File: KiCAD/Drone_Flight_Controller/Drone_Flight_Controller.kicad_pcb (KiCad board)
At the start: 2 copper layers, 0 parts

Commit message: Routing and placing
Routing and placing
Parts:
- added +5V1: +5V, TestPoint:TestPoint_Pad_D1.0mm, F.Cu at (128.4, 56.9)
- added 3V1: 3V3, TestPoint:TestPoint_Pad_D1.0mm, F.Cu at (128.4, 60.0)
- added BZ1: Buzzer, Buzzer_Beeper:Buzzer_TDK_PS1240P02BT_D12.2mm_H6.5mm, F.Cu at (149.0, 74.9)
- added C1: 22u, Capacitor_THT:CP_Radial_D5.0mm_P2.00mm, F.Cu at (139.0, 71.5)
- added C10: 100nF, Capacitor_SMD:C_0805_2012Metric, B.Cu at (170.6, 80.0)
- added C11: 100nF, Capacitor_SMD:C_0805_2012Metric, F.Cu at (153.1, 64.1)
- added C12: 10uF, Capacitor_SMD:C_0805_2012Metric, B.Cu at (181.4, 62.1)
- added C13: 10uF, Capacitor_SMD:C_0805_2012Metric, B.Cu at (187.1, 62.1)
- added C14: 100nF, Capacitor_SMD:C_0805_2012Metric, F.Cu at (171.2, 64.1)
- added C2: 100nF, Capacitor_SMD:C_0805_2012Metric, B.Cu at (156.0, 68.4)
- added C3: 10uF, Capacitor_SMD:C_0805_2012Metric, F.Cu at (186.3, 62.8)
- added C4: 1uF, Capacitor_SMD:C_0805_2012Metric_Pad1.18x1.45mm_HandSolder, B.Cu at (157.7, 76.5)
- added C5: 10uF, Capacitor_SMD:C_0805_2012Metric, B.Cu at (160.0, 68.4)
- added C6: 100nF, Capacitor_SMD:C_0805_2012Metric, F.Cu at (186.3, 60.8)
- added C7: 120n, Capacitor_SMD:C_0805_2012Metric_Pad1.18x1.45mm_HandSolder, B.Cu at (163.1, 72.5)
- added C8: 10uF, Capacitor_SMD:C_0805_2012Metric, B.Cu at (186.7, 82.7)
- added C9: 100nF, Capacitor_SMD:C_0805_2012Metric, B.Cu at (181.2, 82.7)
- added D1: BAT60BE6359HTMA1, Diode_SMD:D_SOD-323_HandSoldering, B.Cu at (164.7, 62.1)
- added D10: LED, LED_SMD:LED_0805_2012Metric_Pad1.15x1.40mm_HandSolder, F.Cu at (161.3, 91.5)
- added D11: LED, LED_SMD:LED_0805_2012Metric_Pad1.15x1.40mm_HandSolder, F.Cu at (164.6, 91.5)
- added D12: LED, LED_SMD:LED_0805_2012Metric_Pad1.15x1.40mm_HandSolder, F.Cu at (167.9, 91.5)
- added D13: LED, LED_SMD:LED_0805_2012Metric_Pad1.15x1.40mm_HandSolder, F.Cu at (171.2, 91.5)
- added D15: LED, LED_SMD:LED_0805_2012Metric_Pad1.15x1.40mm_HandSolder, F.Cu at (155.3, 52.4)
- added D19: LED, LED_SMD:LED_0805_2012Metric_Pad1.15x1.40mm_HandSolder, F.Cu at (151.4, 91.5)
- added D2: BAT60BE6359HTMA1, Diode_SMD:D_SOD-323_HandSoldering, F.Cu at (132.7, 57.0)
- added D3: BAT60BE6359HTMA1, Diode_SMD:D_SOD-323_HandSoldering, F.Cu at (132.7, 88.0)
- added D4: LED, LED_SMD:LED_0805_2012Metric_Pad1.15x1.40mm_HandSolder, F.Cu at (144.8, 91.5)
- added D5: LED, LED_SMD:LED_0805_2012Metric_Pad1.15x1.40mm_HandSolder, F.Cu at (148.1, 91.5)
- added D6: BAT60BE6359HTMA1, Diode_SMD:D_SOD-323_HandSoldering, F.Cu at (183.3, 57.0)
- added D7: BAT60BE6359HTMA1, Diode_SMD:D_SOD-323_HandSoldering, F.Cu at (183.4, 87.9)
- added D8: LED, LED_SMD:LED_0805_2012Metric_Pad1.15x1.40mm_HandSolder, F.Cu at (154.7, 91.5)
- added D9: LED, LED_SMD:LED_0805_2012Metric_Pad1.15x1.40mm_HandSolder, F.Cu at (158.0, 91.5)
- added F1: PTS12066V050, Fuse:Fuse_1206_3216Metric, B.Cu at (159.4, 62.3)
- added F2: PTS12066V050, Fuse:Fuse_1206_3216Metric, F.Cu at (134.9, 57.4)
- added F3: PTS12066V050, Fuse:Fuse_1206_3216Metric, F.Cu at (134.9, 87.7)
- added F4: PTS12066V050, Fuse:Fuse_1206_3216Metric, F.Cu at (181.1, 57.4)
- added F5: PTS12066V050, Fuse:Fuse_1206_3216Metric, F.Cu at (181.2, 87.6)
- added FID1: Fiducial, Fiducial:Fiducial_0.5mm_Mask1mm, F.Cu at (130.6, 58.6)
- added FID2: Fiducial, Fiducial:Fiducial_0.5mm_Mask1mm, F.Cu at (187.0, 87.3)
- added G1: Logo_HTL_Steyr_Small, Symbol_:HTL-Steyr-Logo_5mm_Copper, F.Cu at (369.0, 105.5)
- added GND1: GND, TestPoint:TestPoint_Pad_D1.0mm, F.Cu at (128.4, 63.0)
- added GPS1: Conn_01x04, Connector_PinHeader_2.54mm:PinHeader_1x04_P2.54mm_Vertical, F.Cu at (148.0, 53.0)
- added H1: MountingHole_Pad, MountingHole:MountingHole_2.2mm_M2_Pad_TopBottom, F.Cu at (129.0, 53.5)
- added H2: MountingHole_Pad, MountingHole:MountingHole_2.2mm_M2_Pad_TopBottom, F.Cu at (187.0, 53.5)
- added H3: MountingHole_Pad, MountingHole:MountingHole_2.2mm_M2_Pad_TopBottom, F.Cu at (129.0, 91.5)
- added H4: MountingHole_Pad, MountingHole:MountingHole_2.2mm_M2_Pad_TopBottom, F.Cu at (187.0, 91.5)
- added J1: XT60, Connector_AMASS:AMASS_XT60-F_1x02_P7.20mm_Vertical, F.Cu at (131.5, 76.6)
- added J2: 0.5mΩ high side shunt, Connector_PinHeader_2.54mm:PinHeader_1x02_P2.54mm_Vertical, F.Cu at (144.0, 53.0)
- added J3: Micro_SD_Card, Connector_Card:microSD_HC_Hirose_DM3D-SF, B.Cu at (147.4, 87.2)
- added Motor1: Conn_01x03, Connector_PinHeader_2.54mm:PinHeader_1x03_P2.54mm_Vertical, F.Cu at (133.5, 53.0)
- added Motor2: Conn_01x03, Connector_PinHeader_2.54mm:PinHeader_1x03_P2.54mm_Vertical, F.Cu at (177.5, 53.0)
- added Motor3: Conn_01x03, Connector_PinHeader_2.54mm:PinHeader_1x03_P2.54mm_Vertical, F.Cu at (133.5, 92.0)
- added Motor4: Conn_01x03, Connector_PinHeader_2.54mm:PinHeader_1x03_P2.54mm_Vertical, F.Cu at (177.5, 92.0)
- added Q1: 2N2222A, Package_TO_SOT_THT:TO-92_HandSolder, F.Cu at (138.6, 65.2)
- added R1: 5k1, Resistor_SMD:R_0805_2012Metric_Pad1.20x1.40mm_HandSolder, F.Cu at (158.7, 63.0)
- added R10: 10k, Resistor_SMD:R_0805_2012Metric_Pad1.20x1.40mm_HandSolder, B.Cu at (166.6, 80.0)
- added R11: 220, Resistor_SMD:R_0805_2012Metric_Pad1.20x1.40mm_HandSolder, B.Cu at (170.6, 76.0)
- added R12: 10k, Resistor_SMD:R_0805_2012Metric_Pad1.20x1.40mm_HandSolder, F.Cu at (153.0, 52.4)
- added R13: 3k6, Resistor_SMD:R_0805_2012Metric_Pad1.20x1.40mm_HandSolder, F.Cu at (168.9, 52.4)
- added R14: 1k8, Resistor_SMD:R_0805_2012Metric_Pad1.20x1.40mm_HandSolder, F.Cu at (154.7, 86.5)
- added R15: 1k8, Resistor_SMD:R_0805_2012Metric_Pad1.20x1.40mm_HandSolder, F.Cu at (158.0, 86.5)
- added R16: 1k8, Resistor_SMD:R_0805_2012Metric_Pad1.20x1.40mm_HandSolder, F.Cu at (161.3, 86.5)
- added R17: 1k8, Resistor_SMD:R_0805_2012Metric_Pad1.20x1.40mm_HandSolder, F.Cu at (164.6, 86.6)
- added R18: 1k8, Resistor_SMD:R_0805_2012Metric_Pad1.20x1.40mm_HandSolder, F.Cu at (167.9, 86.5)
- added R19: 1k8, Resistor_SMD:R_0805_2012Metric_Pad1.20x1.40mm_HandSolder, F.Cu at (171.2, 86.5)
- added R2: 5k1, Resistor_SMD:R_0805_2012Metric_Pad1.20x1.40mm_HandSolder, F.Cu at (165.6, 63.0)
- added R24: 1k8, Resistor_SMD:R_0805_2012Metric_Pad1.20x1.40mm_HandSolder, F.Cu at (151.4, 86.5)
- added R25: 10k, Resistor_SMD:R_0805_2012Metric_Pad1.20x1.40mm_HandSolder, B.Cu at (141.6, 78.1)
- added R26: 10k, Resistor_SMD:R_0805_2012Metric_Pad1.20x1.40mm_HandSolder, B.Cu at (144.6, 78.1)
- added R27: 10k, Resistor_SMD:R_0805_2012Metric_Pad1.20x1.40mm_HandSolder, B.Cu at (147.5, 78.1)
- added R28: 10k, Resistor_SMD:R_0805_2012Metric_Pad1.20x1.40mm_HandSolder, B.Cu at (150.4, 78.1)
- added R29: 10k, Resistor_SMD:R_0805_2012Metric_Pad1.20x1.40mm_HandSolder, B.Cu at (153.4, 78.1)
- added R3: 180, Resistor_SMD:R_0805_2012Metric_Pad1.20x1.40mm_HandSolder, B.Cu at (148.5, 66.5)
- added R4: 1k, Resistor_SMD:R_0805_2012Metric_Pad1.20x1.40mm_HandSolder, B.Cu at (143.5, 66.5)
- added R5: 1k8, Resistor_SMD:R_0805_2012Metric_Pad1.20x1.40mm_HandSolder, F.Cu at (144.8, 86.5)
- added R6: 3k6, Resistor_SMD:R_0805_2012Metric_Pad1.20x1.40mm_HandSolder, F.Cu at (148.1, 86.5)
- added R7: 10k, Resistor_SMD:R_0805_2012Metric_Pad1.20x1.40mm_HandSolder, B.Cu at (162.1, 76.5)
- added R8: 10k, Resistor_SMD:R_0805_2012Metric_Pad1.20x1.40mm_HandSolder, F.Cu at (171.2, 52.4)
- added R9: 43k, Resistor_SMD:R_0805_2012Metric_Pad1.20x1.40mm_HandSolder, B.Cu at (166.6, 76.0)
- added SW1: SW_Push, htl_smd:SW_Push_5.1mm_H1.5mm, F.Cu at (171.2, 58.1)
- added SW2: SW_Push, htl_smd:SW_Push_5.1mm_H1.5mm, F.Cu at (153.1, 58.1)
- added U1: 74AHC1G125, Package_TO_SOT_SMD:SOT-353_SC-70-5, F.Cu at (137.8, 56.5)
- added U2: 74AHC1G125, Package_TO_SOT_SMD:SOT-353_SC-70-5, F.Cu at (137.7, 88.6)
- added U3: 74AHC1G125, Package_TO_SOT_SMD:SOT-353_SC-70-5, F.Cu at (178.2, 56.4)
- added U4: 74AHC1G125, Package_TO_SOT_SMD:SOT-353_SC-70-5, F.Cu at (178.3, 88.5)
- added U5: BNO055, Package_LGA:LGA-28_5.2x3.8mm_P0.5mm, B.Cu at (158.0, 72.5)
- added U6: ESP32-S3-MINI-1, RF_Module_:ESP32-S3-MINI-1, F.Cu at (181.3, 72.5)
- added U7: DPS368, Package_LGA:Bosch_LGA-8_2x2.5mm_P0.65mm_ClockwisePinNumbering, B.Cu at (184.0, 82.7)
- added U8: TLV75533PDBV, Package_TO_SOT_SMD:SOT-23-5, B.Cu at (184.2, 62.1)
- added U9: INA195, Package_TO_SOT_SMD:SOT-23-5, B.Cu at (143.0, 60.0)
- added USB-C1: USB_C_Receptacle_USB2.0_14P, Connector_USB:USB_C_Receptacle_HRO_TYPE-C-31-M-12, F.Cu at (162.1, 54.4)
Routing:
- net +3V3: track 0.00 -> 204.1 mm, vias 0 -> 3
- net +5V: track 0.00 -> 200.2 mm, vias 0 -> 2
- net SDI: track 0.00 -> 73.4 mm, vias 0 -> 3
- net Motor3: track 0.00 -> 71.3 mm, vias 0 -> 2
- net SDO: track 0.00 -> 64.7 mm, vias 0 -> 3
- net Motor1: track 0.00 -> 56.9 mm, vias 0 -> 4
- net SD_CS: track 0.00 -> 55.1 mm, vias 0 -> 1
- net EN: track 0.00 -> 53.9 mm, vias 0 -> 2
- net SCK: track 0.00 -> 53.0 mm, vias 0 -> 4
- net LED6: track 0.00 -> 48.1 mm, vias 0 -> 2
- net LED5: track 0.00 -> 46.5 mm, vias 0 -> 2
- net LED4: track 0.00 -> 44.2 mm, vias 0 -> 2
- net CurrentSense: track 0.00 -> 43.7 mm, vias 0 -> 1
- net LED7: track 0.00 -> 43.6 mm, vias 0 -> 2
- net LED3: track 0.00 -> 41.7 mm, vias 0 -> 2
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- added copper zone on B.Cu, net GND
- added copper zone on F.Cu, net GND
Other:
- board outline added: 65 x 45 mm

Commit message: Revision
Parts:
- moved +5V 0.72 mm to (129.0, 57.3)
- moved 3V3 0.72 mm to (129.0, 60.4)
- moved GND 0.72 mm to (129.0, 63.4)
- moved U7 0.10 mm to (183.9, 82.8)
- renumbered +5V1 to +5V, 3V1 to 3V3, GND1 to GND
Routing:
- net +3V3: track 204.1 -> 200.0 mm

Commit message: Add signage
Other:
- board text added: "3V3"
- board text added: "5V"
- board text added: "BOOT"
- board text added: "RESET"

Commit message: routing
routing
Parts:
- moved F3 4.77 mm to (139.5, 86.7)
- moved F2 4.71 mm to (139.5, 58.3)
- moved D3 4.48 mm to (137.0, 87.0)
- moved D2 4.44 mm to (137.0, 58.0)
- moved U2 4.27 mm to (133.6, 87.6), turned to 0 degrees
- moved U1 4.27 mm to (133.6, 57.4), turned to 0 degrees
- moved F4 2.59 mm to (183.5, 58.3)
- moved D7 2.53 mm to (181.0, 87.0)
- moved F5 2.50 mm to (183.5, 86.7)
- moved D6 2.48 mm to (181.0, 58.0)
- moved R8 2.00 mm to (173.1, 53.1)
- moved R12 1.84 mm to (151.3, 53.1)
- moved FID1 1.72 mm to (130.8, 60.3)
- moved R3 1.50 mm to (147.0, 66.5)
- moved U3 1.22 mm to (177.5, 57.4)
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- renumbered GPS1 to GPS, USB-C1 to USB-C
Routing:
- net +5V: track 199.7 -> 180.4 mm
- net GPS TX: track 34.1 -> 40.2 mm
- net GPS RX: track 32.9 -> 38.1 mm
- net Motor1: track 56.9 -> 62.0 mm
- net Net-(Motor3-Pin_1): track 9.30 -> 4.18 mm, vias 1 -> 0
- net +3V3: track 200.0 -> 204.9 mm
- net Net-(Motor4-Pin_1): track 8.77 -> 4.18 mm, vias 1 -> 0
- net Net-(Motor1-Pin_1): track 10.1 -> 5.73 mm, vias 1 -> 0
- net Motor3: track 71.3 -> 74.7 mm, vias 2 -> 4
- net Net-(C14-Pad1): track 12.4 -> 10.4 mm
- net Net-(Q1-B): track 9.06 -> 7.06 mm
- net Buzzer: track 29.5 -> 31.5 mm
- net Net-(Motor2-Pin_1): track 7.17 -> 5.56 mm, vias 1 -> 0
- net Net-(BZ1--): track 15.2 -> 13.6 mm
- net D-: track 23.5 -> 25.0 mm
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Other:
- board text removed: "BOOT"

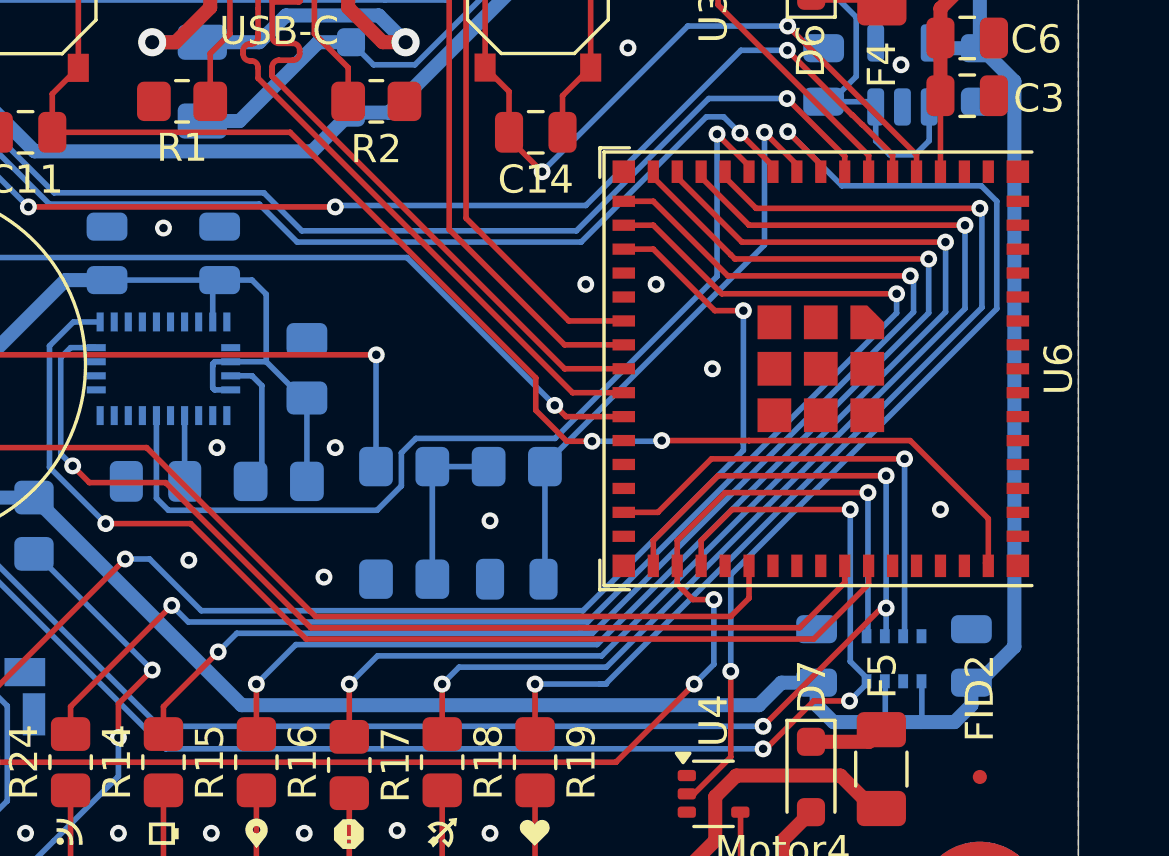
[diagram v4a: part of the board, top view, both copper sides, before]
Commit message: Shorten traces
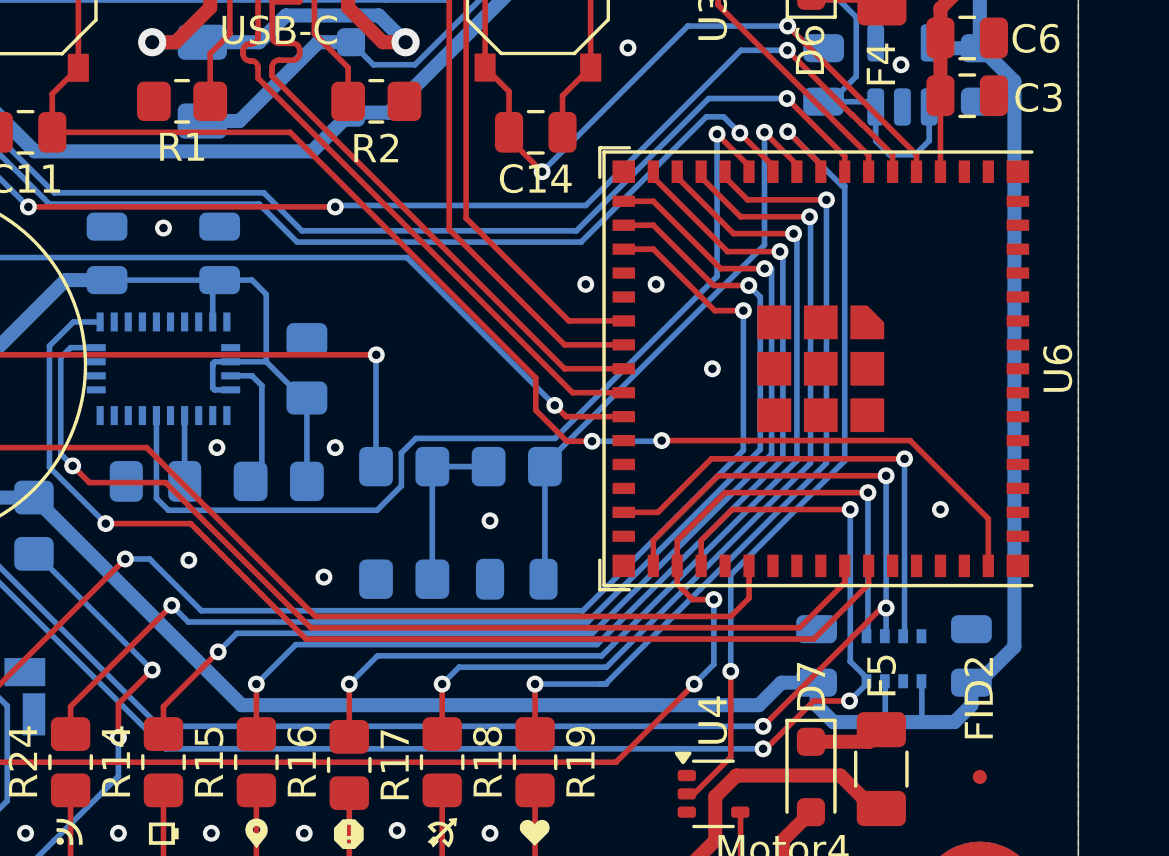
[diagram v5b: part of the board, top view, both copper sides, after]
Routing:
- net LED1: track 36.7 -> 29.1 mm
- net LED2: track 39.1 -> 31.7 mm
- net Motor4: track 36.1 -> 28.8 mm
- net LED4: track 44.2 -> 37.0 mm
- net LED3: track 41.7 -> 34.6 mm
- net LED6: track 48.1 -> 41.1 mm
- net LED5: track 46.5 -> 39.6 mm

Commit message: Update Signage
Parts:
- removed G1: Logo_HTL_Steyr_Small, Symbol_:HTL-Steyr-Logo_5mm_Copper
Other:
- board text added: "Flight Controller V3 Brandner, Hinterberger TOP GND"

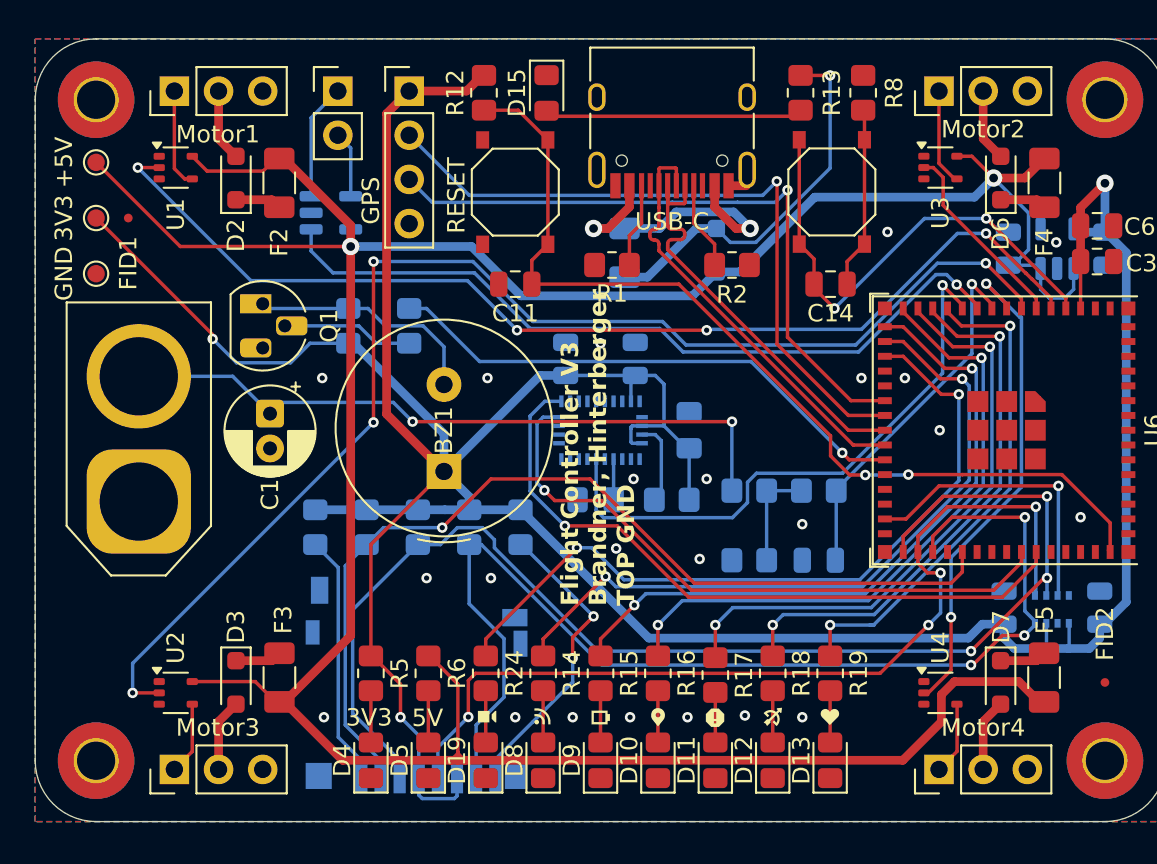
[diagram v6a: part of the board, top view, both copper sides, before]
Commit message: Mark GND on connectors
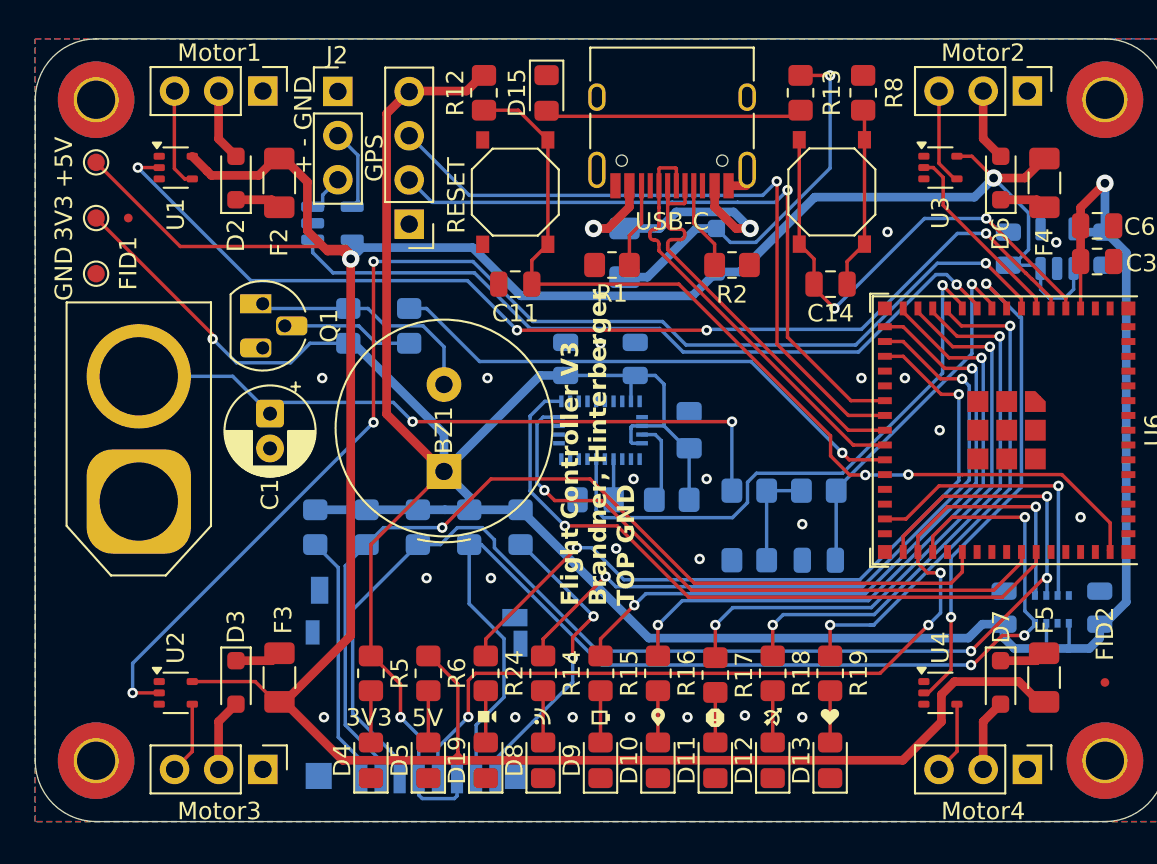
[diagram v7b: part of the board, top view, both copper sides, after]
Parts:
- J2: footprint Connector_PinHeader_2.54mm:PinHeader_1x02_P2.54mm_Vertical -> Connector_PinHeader_2.54mm:PinHeader_1x03_P2.54mm_Vertical
- moved GPS 7.65 mm to (147.0, 60.6), turned to 180 degrees
- moved Motor1 5.09 mm to (138.6, 53.0), turned to -90 degrees
- moved Motor3 5.09 mm to (138.6, 92.0), turned to -90 degrees
- moved Motor2 5.08 mm to (182.5, 53.0), turned to -90 degrees
- moved Motor4 5.08 mm to (182.5, 92.0), turned to -90 degrees
- moved U9 0.61 mm to (142.6, 60.6)
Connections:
- GPS pad 1: +3V3 -> GND
- GPS pad 2: GPS TX -> GPS RX
- GPS pad 3: GPS RX -> GPS TX
- GPS pad 4: GND -> +3V3
- J2 pad 1: Net-(J2-Pin_1) -> GND
- Motor1 pad 1: Net-(Motor1-Pin_1) -> GND
- Motor1 pad 3: GND -> Net-(Motor1-Pin_3)
- Motor2 pad 1: Net-(Motor2-Pin_1) -> GND
- Motor2 pad 3: GND -> Net-(Motor2-Pin_3)
- Motor3 pad 1: Net-(Motor3-Pin_1) -> GND
- Motor3 pad 3: GND -> Net-(Motor3-Pin_3)
- Motor4 pad 1: Net-(Motor4-Pin_1) -> GND
- Motor4 pad 3: GND -> Net-(Motor4-Pin_3)
- U1 pad 4: Net-(Motor1-Pin_1) -> Net-(Motor1-Pin_3)
- U2 pad 4: Net-(Motor3-Pin_1) -> Net-(Motor3-Pin_3)
- U3 pad 4: Net-(Motor2-Pin_1) -> Net-(Motor2-Pin_3)
- U4 pad 4: Net-(Motor4-Pin_1) -> Net-(Motor4-Pin_3)
- U9 pad 3: Net-(J2-Pin_1) -> Net-(J2-Pin_3)
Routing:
- net Net-(J2-Pin_1): track 7.49 -> 0.00 mm
- net Net-(Motor1-Pin_3): track 0.00 -> 5.73 mm
- net Net-(Motor1-Pin_1): track 5.73 -> 0.00 mm
- net Net-(Motor2-Pin_3): track 0.00 -> 5.56 mm
- net Net-(Motor2-Pin_1): track 5.56 -> 0.00 mm
- net Net-(Motor4-Pin_3): track 0.00 -> 4.18 mm
- net Net-(Motor4-Pin_1): track 4.18 -> 0.00 mm
- net Net-(Motor3-Pin_3): track 0.00 -> 4.18 mm
- net Net-(Motor3-Pin_1): track 4.18 -> 0.00 mm
- net Net-(J2-Pin_3): track 0.00 -> 2.51 mm
- net +5V: track 180.4 -> 182.8 mm
- net Net-(J2-Pin_2): track 3.82 -> 4.72 mm
- net GND: track 1.01 -> 1.82 mm
- net CurrentSense: track 44.7 -> 44.1 mm
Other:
- board text added: "+ - GND"

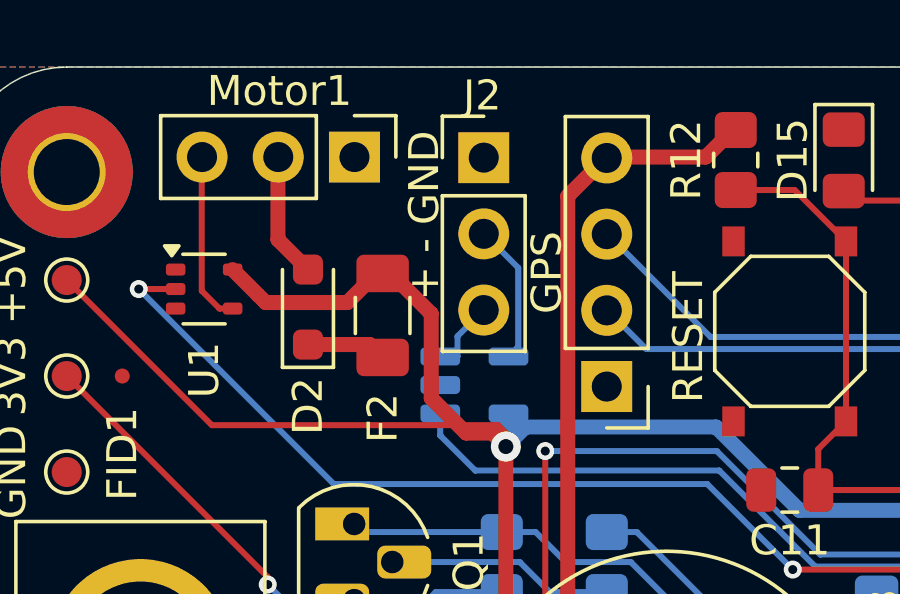
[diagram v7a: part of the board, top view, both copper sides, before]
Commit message: Add resistor parallel to shunt to lower EMI
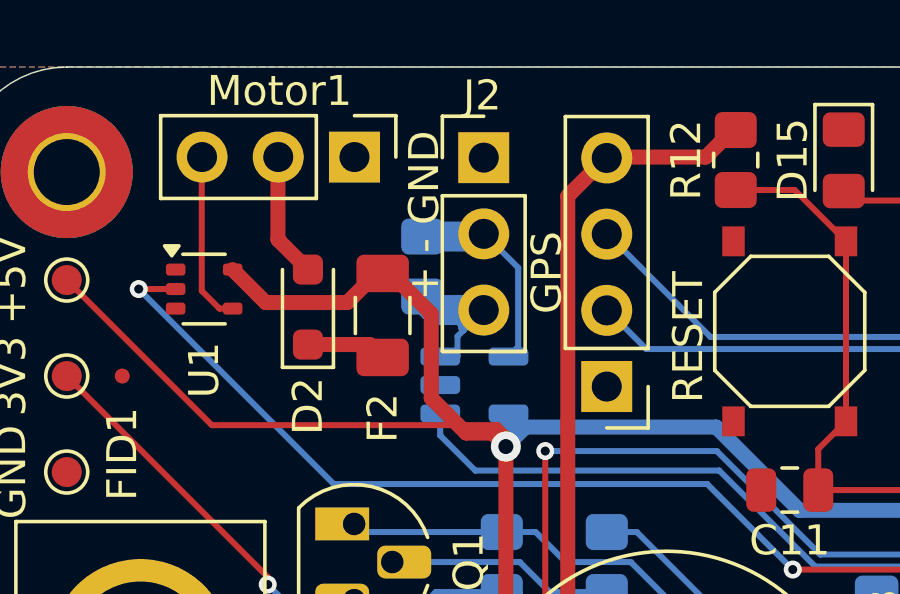
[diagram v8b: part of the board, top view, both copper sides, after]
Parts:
- added R20: 24, Resistor_SMD:R_0805_2012Metric_Pad1.20x1.40mm_HandSolder, B.Cu at (140.8, 56.6)
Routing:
- net Net-(J2-Pin_3): track 2.51 -> 6.11 mm
- net Net-(J2-Pin_2): track 4.72 -> 6.81 mm
